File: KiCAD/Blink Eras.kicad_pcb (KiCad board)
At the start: 2 copper layers, 27.9 x 20.3 mm, 12 parts, among them P1 ISP, U1 ICM7555, U2 ATTINY85-M

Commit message: Artwork, first draft..
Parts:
- added G***: LOGO, BlinkyFeet:555-lettering, F.Cu at (137.2, 94.0)
- added G***: LOGO, BlinkyFeet:AVR-lettering, F.Cu at (152.4, 94.0)
- added G***: LOGO, BlinkyFeet:Nixon-image, F.Cu at (135.9, 95.2)
- added G***: LOGO, BlinkyFeet:Clinton-image, F.Cu at (153.7, 95.2)

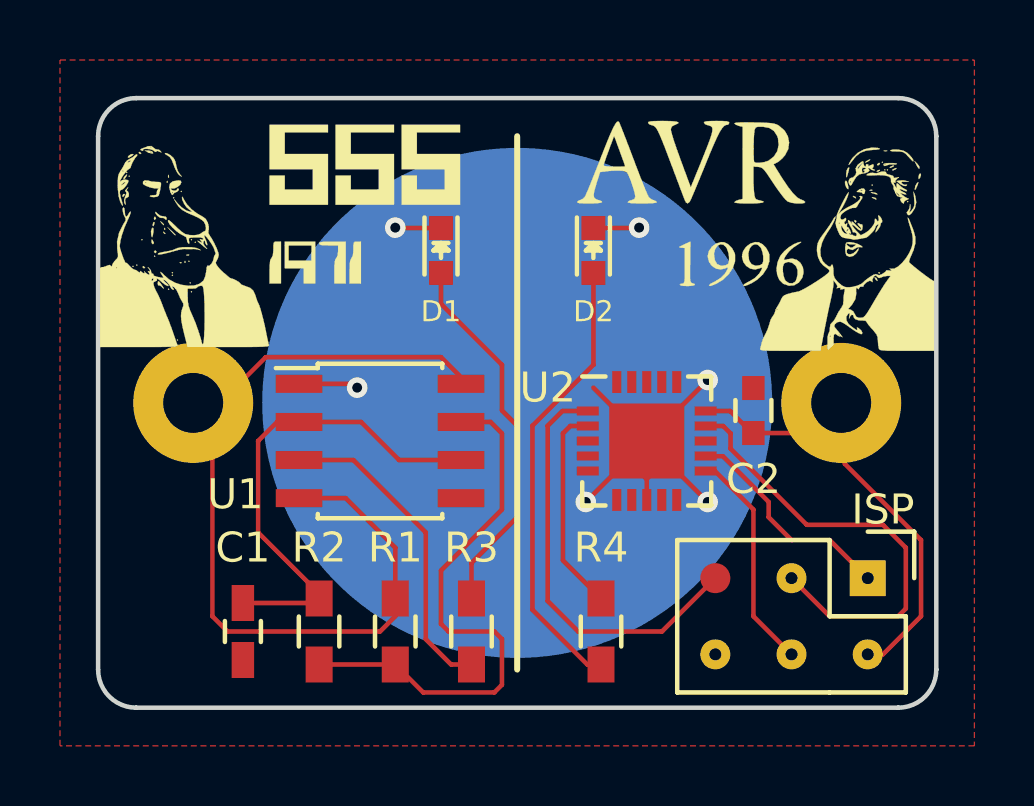
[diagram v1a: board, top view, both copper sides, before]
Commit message: Updated all artwork.  Many layers.
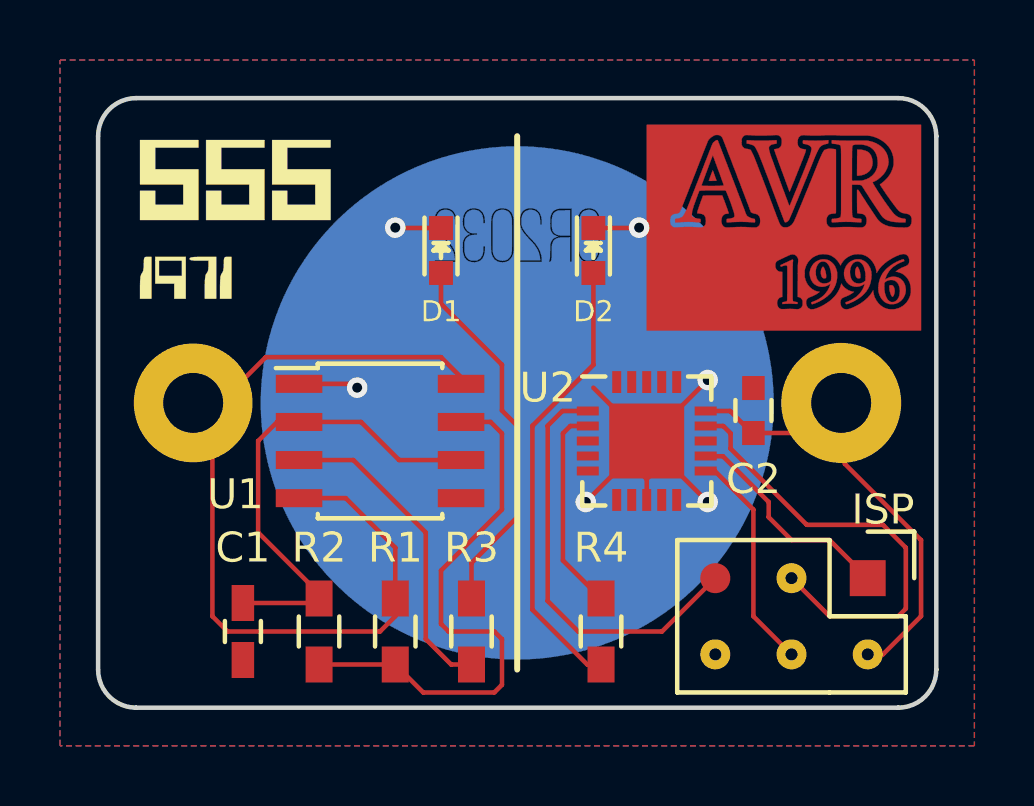
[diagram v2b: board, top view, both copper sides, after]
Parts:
- removed the G*** at (152.4, 94.0)
- removed the G*** at (135.9, 95.2)
- removed the G*** at (153.7, 95.2)
- added G***: LOGO, BlinkyFeet:AVR 1996, F.Cu at (153.7, 94.5)
- added G***: LOGO, BlinkyFeet:AVR 1996 dilated, F.Cu at (153.7, 94.5)
- added G***: LOGO, BlinkyFeet:AVR 1996 double dilated, F.Cu at (153.7, 94.5)
- added G***: LOGO, BlinkyFeet:Nixon-left, B.Cu at (135.9, 107.2)
- added G***: LOGO, BlinkyFeet:Clinton-right, B.Cu at (153.7, 107.2)
- BT1: footprint BlinkyFeet:BK-913 -> BlinkyFeet:Big_Pad_Battery
- moved G*** 4.35 mm to (132.8, 94.5)
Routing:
- added copper zone on B.Cu, net VCC
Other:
- board text added: "Blink Eras 1.0"

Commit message: v1.1 changes
 - Shrink through holes for battery clip.
 - Eliminate rectangle around "AVR" lettering.
 - Change "555" and "1971" lettering to get better separation.
 - Enlarge "CR2032" lettering.
 - Enlarge presidents' caricatures, just keep the faces.
 - Increment the silkscreen version number.
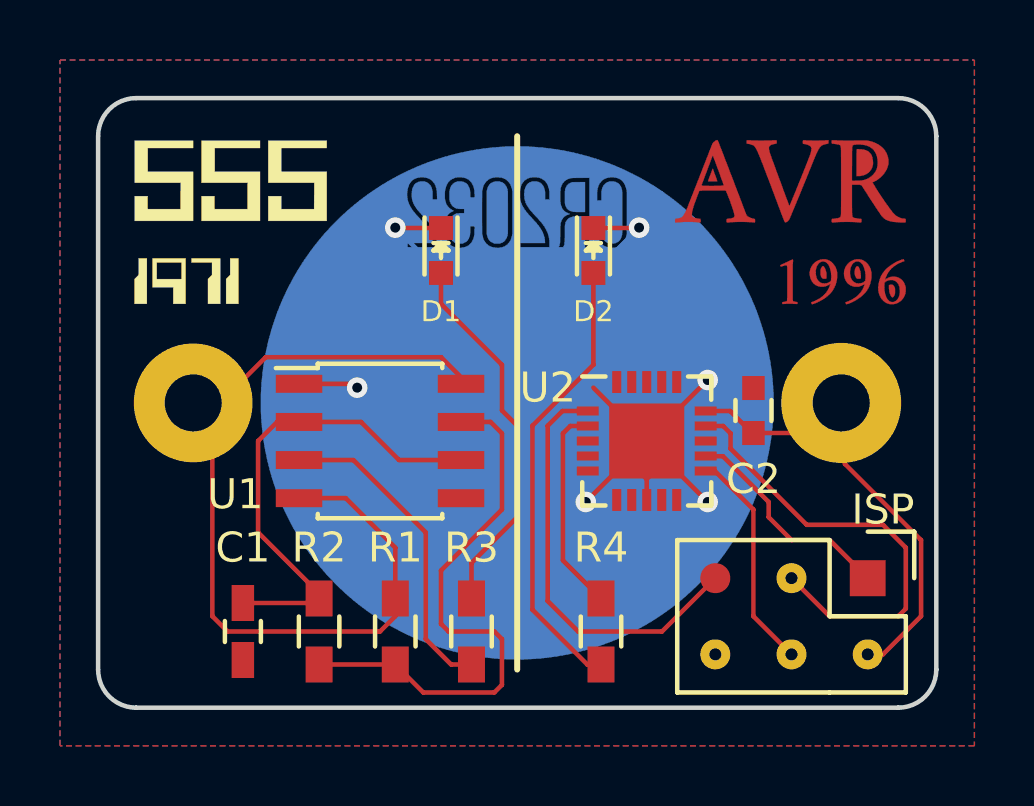
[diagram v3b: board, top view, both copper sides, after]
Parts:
- removed the G*** at (153.7, 94.5)
- G***: footprint BlinkyFeet:555-lettering -> BlinkyFeet:555 1971
- moved G*** 3.30 mm to (136.1, 94.5)
- moved G*** 1.93 mm to (137.7, 108.0)
- moved G*** 1.93 mm to (151.9, 108.0)
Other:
- board text added: "Blink Eras 1.1"
- board text removed: "Blink Eras 1.0"
